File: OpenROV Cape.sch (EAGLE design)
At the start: 51 parts, among them IC1 ATMEGA328P-PU, IC2 V_REG_317SMD, Q1 MOSFET-NCHANNELSMD, Q2 MOSFET-NCHANNELSMD, Q3 MOSFET-NCHANNELSMD, U1 ARDUINO_SHIELDNO_SILK, Y1 16Mhz

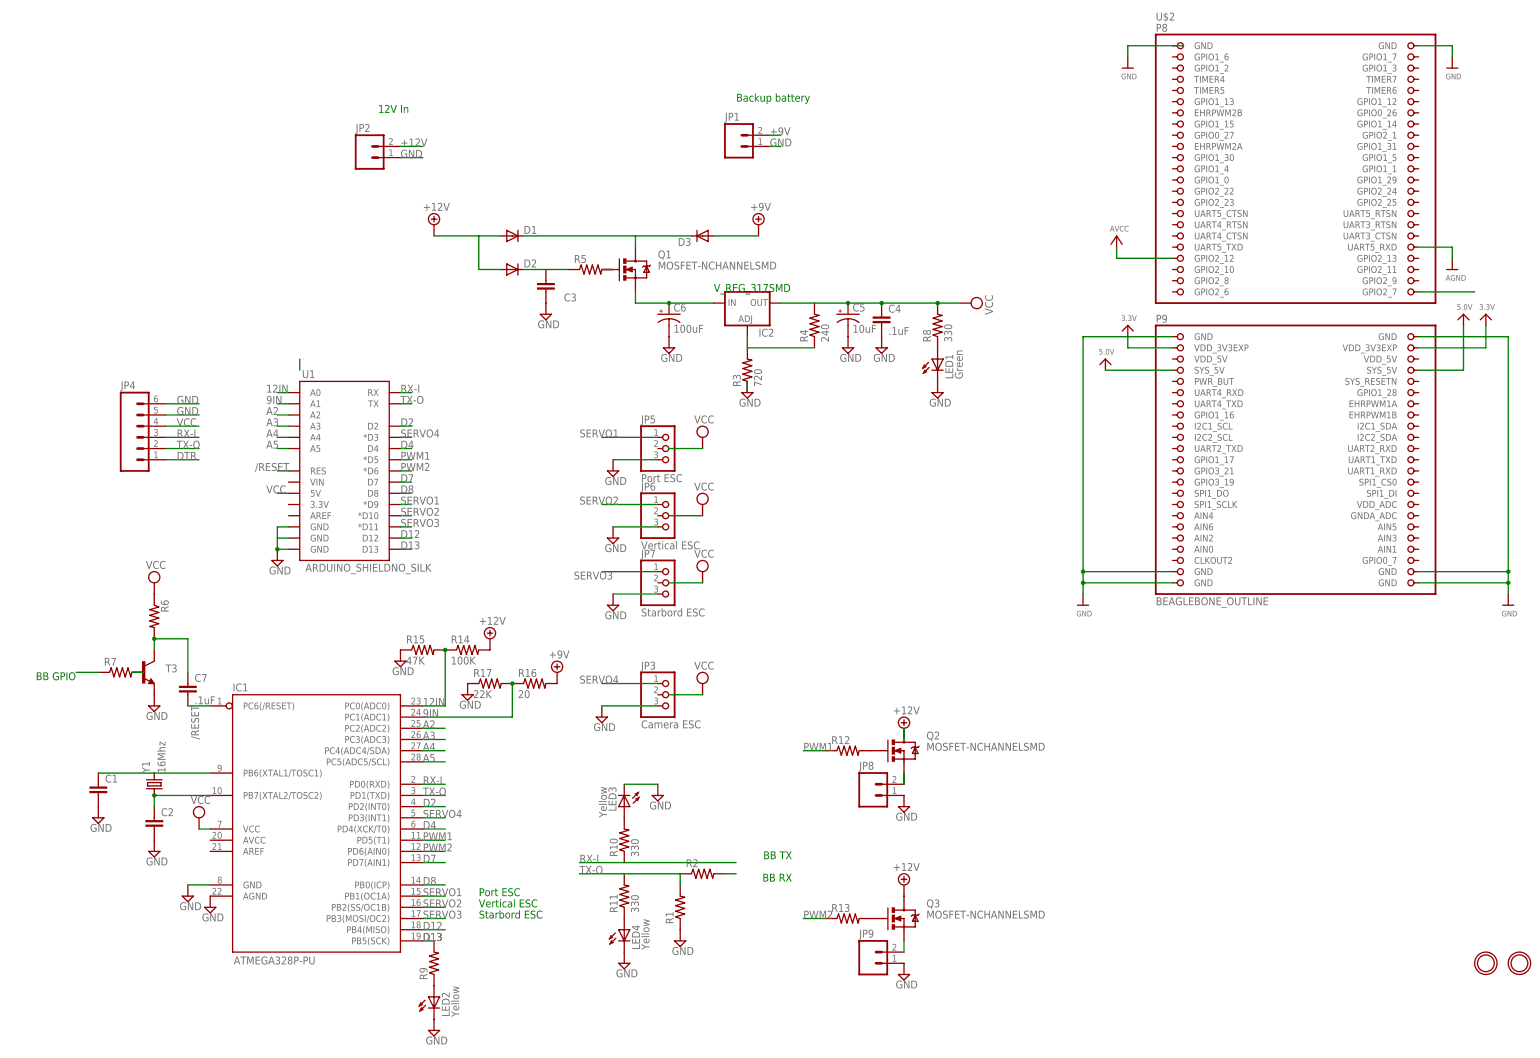
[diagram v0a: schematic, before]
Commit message: Added values and fixed errors
Added/ corrected values to most components, corrected erroneous voltage
divider configuration to TX-O, added resister between BBTX and RX-I,
changed sheet labels
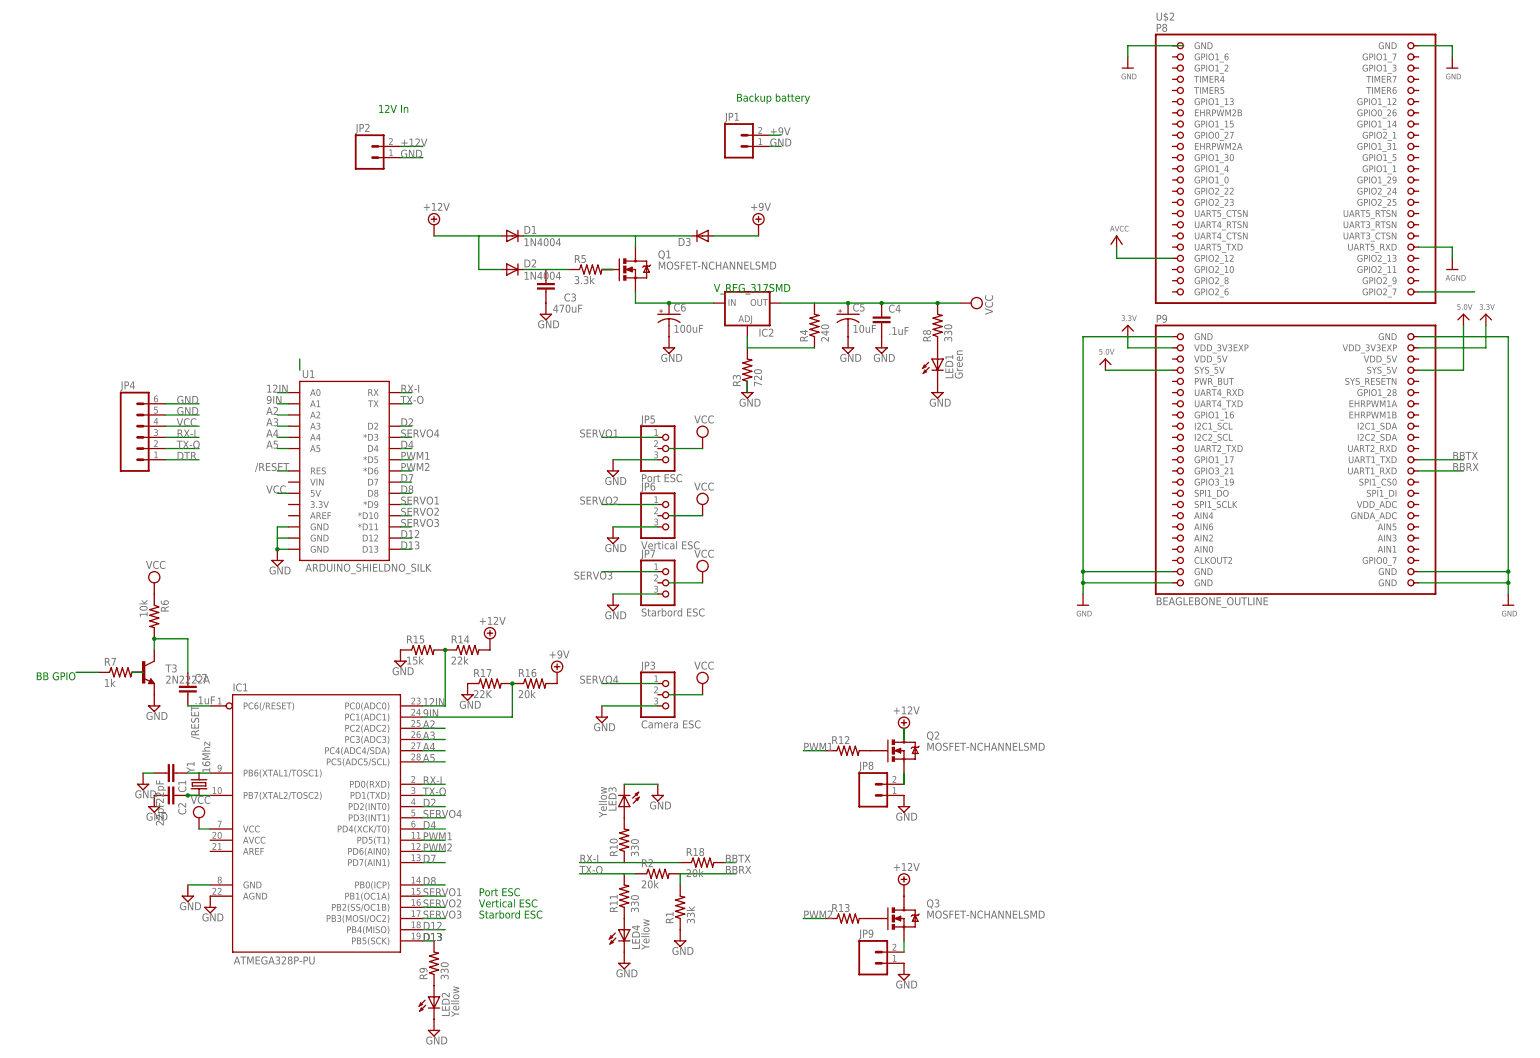
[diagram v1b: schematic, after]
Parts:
- removed U$22, U$23: MOUNTINGHOLE3.0THIN, microbuilder:MOUNTINGHOLE3.0THIN
- added R18: 20k, SparkFun-Passives:RESISTOR0805-RES
- C1, C2: value (none) -> 22pF
- C3: value (none) -> 470uF
- D1, D2: value (none) -> 1N4004
- R1: value (none) -> 33k
- R14: value 100K -> 22k
- R15: value 47K -> 15k
- R16: value 20 -> 20k
- R2: value (none) -> 20k
- R5: value (none) -> 3.3k
- R6: value (none) -> 10k
- R7: value (none) -> 1k
- R9: value (none) -> 330
- T3: value (none) -> 2N2222A
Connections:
- removed net N$2: R2.2
- new net BBRX: R1.2, R2.2, U$2.UART1_RXD
- new net BBTX: R18.2, U$2.UART1_TXD
- net RX-I: now also R18.1
- net TX-O: no longer R1.2
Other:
- note removed: "BB RX"
- note removed: "BB TX"
- moved on the sheet: C1, C2, R2, Y1

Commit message: Disambiguated several features
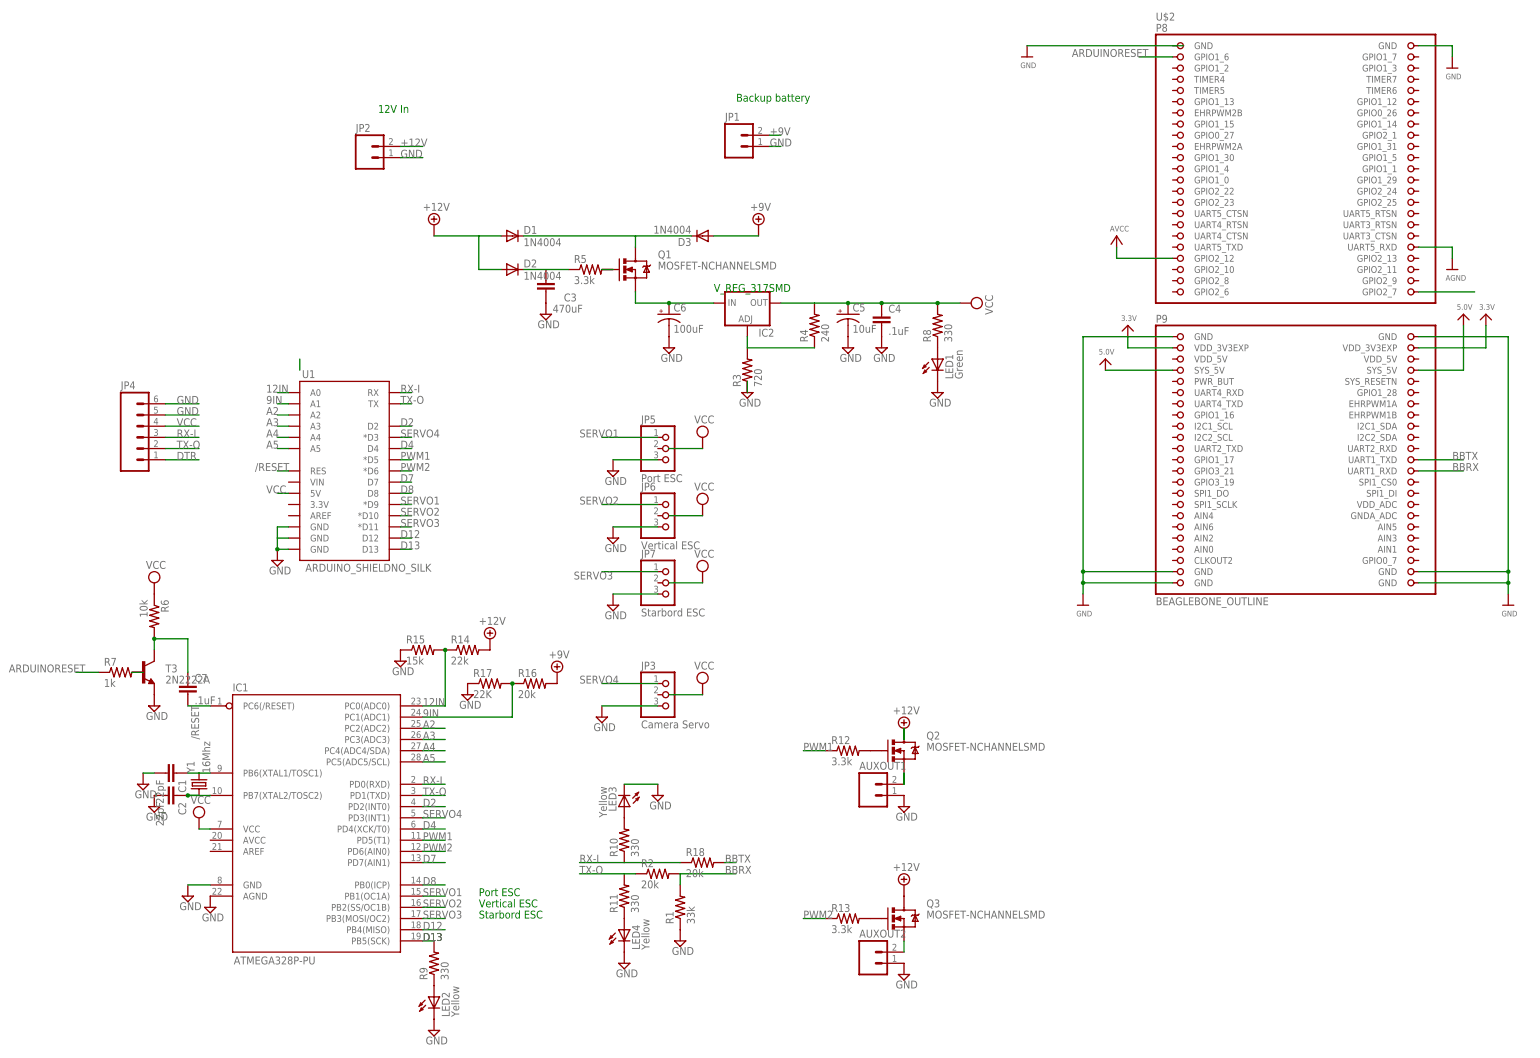
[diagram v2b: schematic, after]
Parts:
- D3: value (none) -> 1N4004
- JP3: value Camera ESC -> Camera Servo
- R12, R13: value (none) -> 3.3k
- renumbered JP8 to AUXOUT1, JP9 to AUXOUT2
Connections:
- removed net N$6: R7.1
- new net ARDUINORESET: R7.1, U$2.GPIO1_6
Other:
- note removed: "BB GPIO"
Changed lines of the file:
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@@
 <part name="C3" library="SparkFun-Passives" deviceset="CAP" device="0805" value="470uF"/>
 <part name="SUPPLY9" library="supply2" deviceset="GND" device=""/>
-<part name="D3" library="SparkFun-DiscreteSemi" deviceset="DIODE" device="SMA"/>
+<part name="D3" library="SparkFun-DiscreteSemi" deviceset="DIODE" device="SMA" value="1N4004"/>
 <part name="IC2" library="SparkFun-PowerIC" deviceset="V_REG_317" device="SMD" value=""/>
 <part name="SUPPLY10" library="supply2" deviceset="GND" device=""/>
@@
 <part name="JP2" library="SparkFun" deviceset="M02" device="PTH"/>
 <part name="Q1" library="SparkFun-DiscreteSemi" deviceset="MOSFET-NCHANNEL" device="SMD"/>
-<part name="JP3" library="pinhead" deviceset="PINHD-1X3" device="" value="Camera ESC"/>
+<part name="JP3" library="pinhead" deviceset="PINHD-1X3" device="" value="Camera Servo"/>
 <part name="SUPPLY6" library="supply2" deviceset="VCC" device=""/>
 <part name="SUPPLY14" library="supply2" deviceset="GND" device=""/>
@@
 <part name="SUPPLY27" library="supply2" deviceset="GND" device=""/>
 <part name="SUPPLY28" library="supply2" deviceset="GND" device=""/>
-<part name="JP8" library="SparkFun" deviceset="M02" device="PTH"/>
+<part name="AUXOUT1" library="SparkFun" deviceset="M02" device="PTH"/>
 <part name="Q2" library="SparkFun-DiscreteSemi" deviceset="MOSFET-NCHANNEL" device="SMD"/>
 <part name="SUPPLY29" library="supply2" deviceset="+12V" device=""/>
-<part name="R12" library="SparkFun-Passives" deviceset="RESISTOR" device="0805-RES"/>
+<part name="R12" library="SparkFun-Passives" deviceset="RESISTOR" device="0805-RES" value="3.3k"/>
 <part name="SUPPLY30" library="supply2" deviceset="GND" device=""/>
-<part name="JP9" library="SparkFun" deviceset="M02" device="PTH"/>
+<part name="AUXOUT2" library="SparkFun" deviceset="M02" device="PTH"/>
 <part name="SUPPLY31" library="supply2" deviceset="GND" device=""/>
 <part name="Q3" library="SparkFun-DiscreteSemi" deviceset="MOSFET-NCHANNEL" device="SMD"/>
-<part name="R13" library="SparkFun-Passives" deviceset="RESISTOR" device="0805-RES"/>
+<part name="R13" library="SparkFun-Passives" deviceset="RESISTOR" device="0805-RES" value="3.3k"/>
 <part name="SUPPLY32" library="supply2" deviceset="+12V" device=""/>
 <part name="R14" library="SparkFun-Passives" deviceset="RESISTOR" device="0805-RES" value="22k"/>
@@
 <text x="142.24" y="45.72" size="1.778" layer="91">Vertical ESC</text>
 <text x="142.24" y="43.18" size="1.778" layer="91">Starbord ESC</text>
-<text x="50.8" y="99.06" size="1.778" layer="91" rot="R180">BB GPIO</text>
 <text x="200.66" y="228.6" size="1.778" layer="91">Backup battery</text>
 <text x="119.38" y="226.06" size="1.778" layer="91">12V In</text>
@@
 <instance part="U$12" gate="G$1" x="279.4" y="114.3"/>
 <instance part="U$13" gate="G$1" x="375.92" y="114.3"/>
-<instance part="U$14" gate="G$1" x="289.56" y="236.22"/>
+<instance part="U$14" gate="G$1" x="266.7" y="238.76"/>
 <instance part="U$15" gate="G$1" x="363.22" y="236.22"/>
 <instance part="U$3" gate="G$1" x="284.48" y="167.64"/>
@@
 <instance part="SUPPLY27" gate="GND" x="175.26" y="33.02"/>
 <instance part="SUPPLY28" gate="GND" x="182.88" y="71.12"/>
-<instance part="JP8" gate="G$1" x="231.14" y="71.12"/>
+<instance part="AUXOUT1" gate="G$1" x="231.14" y="71.12"/>
 <instance part="Q2" gate="G$1" x="238.76" y="81.28"/>
 <instance part="SUPPLY29" gate="+12V" x="238.76" y="86.36"/>
 <instance part="R12" gate="G$1" x="226.06" y="81.28"/>
 <instance part="SUPPLY30" gate="GND" x="238.76" y="68.58"/>
-<instance part="JP9" gate="G$1" x="231.14" y="33.02"/>
+<instance part="AUXOUT2" gate="G$1" x="231.14" y="33.02"/>
 <instance part="SUPPLY31" gate="GND" x="238.76" y="30.48"/>
 <instance part="Q3" gate="G$1" x="238.76" y="43.18"/>
@@
 </segment>
 <segment>
-<wire x1="302.26" y1="241.3" x2="289.56" y2="241.3" width="0.1524" layer="91"/>
 <pinref part="U$14" gate="G$1" pin="GND"/>
-<wire x1="289.56" y1="241.3" x2="289.56" y2="238.76" width="0.1524" layer="91"/>
+<wire x1="302.26" y1="241.3" x2="266.7" y2="241.3" width="0.1524" layer="91"/>
 </segment>
 <segment>
@@
 </segment>
 <segment>
-<pinref part="JP8" gate="G$1" pin="1"/>
+<pinref part="AUXOUT1" gate="G$1" pin="1"/>
 <pinref part="SUPPLY30" gate="GND" pin="GND"/>
 </segment>
 <segment>
-<pinref part="JP9" gate="G$1" pin="1"/>
+<pinref part="AUXOUT2" gate="G$1" pin="1"/>
 <pinref part="SUPPLY31" gate="GND" pin="GND"/>
 </segment>
@@
 </segment>
 </net>
-<net name="N$6" class="0">
-<segment>
-<wire x1="55.88" y1="99.06" x2="50.8" y2="99.06" width="0.1524" layer="91"/>
-<pinref part="R7" gate="G$1" pin="1"/>
-</segment>
-</net>
 <net name="BBRX" class="0">
 <segment>
@@
 <net name="N$12" class="0">
 <segment>
-<pinref part="JP8" gate="G$1" pin="2"/>
+<pinref part="AUXOUT1" gate="G$1" pin="2"/>
 <pinref part="Q2" gate="G$1" pin="S"/>
 <wire x1="238.76" y1="73.66" x2="238.76" y2="76.2" width="0.1524" layer="91"/>
@@
 <net name="N$14" class="0">
 <segment>
-<pinref part="JP9" gate="G$1" pin="2"/>
+<pinref part="AUXOUT2" gate="G$1" pin="2"/>
 <pinref part="Q3" gate="G$1" pin="S"/>
 <wire x1="238.76" y1="35.56" x2="238.76" y2="38.1" width="0.1524" layer="91"/>
@@
 </segment>
 </net>
+<net name="ARDUINORESET" class="0">
+<segment>
+<pinref part="U$2" gate="G$1" pin="GPIO1_6"/>
+<wire x1="299.72" y1="238.76" x2="292.1" y2="238.76" width="0.1524" layer="91"/>
+<label x="276.86" y="238.76" size="1.778" layer="95"/>
+</segment>
+<segment>
+<wire x1="55.88" y1="99.06" x2="50.8" y2="99.06" width="0.1524" layer="91"/>
+<pinref part="R7" gate="G$1" pin="1"/>
+<label x="35.56" y="99.06" size="1.778" layer="95"/>
+</segment>
+</net>
